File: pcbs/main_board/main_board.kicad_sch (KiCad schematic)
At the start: 6 parts, among them J3 LED strip, J4 Motor, P1 USB/STEPUP, U1 mini_esp32

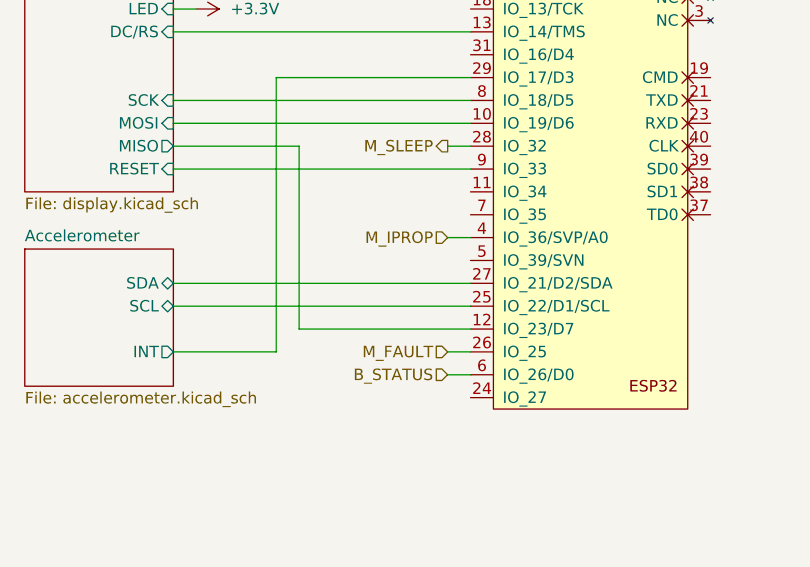
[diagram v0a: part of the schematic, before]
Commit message: Changed pinout
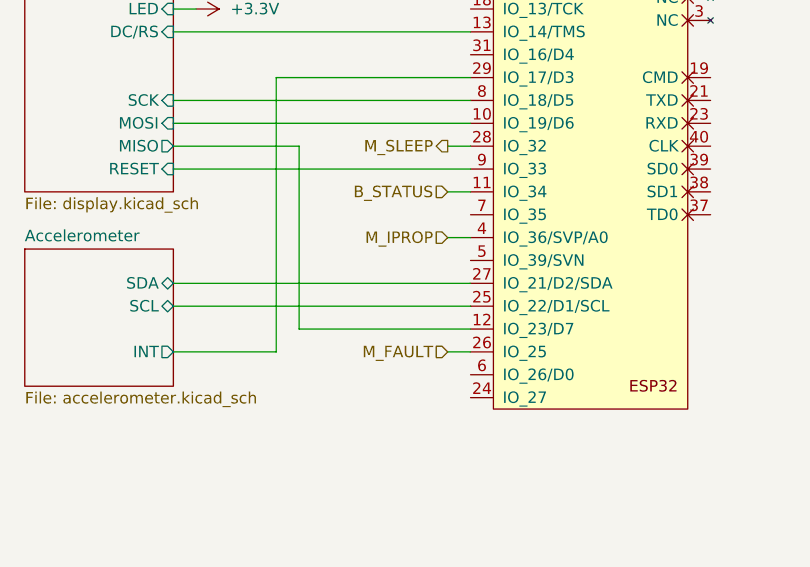
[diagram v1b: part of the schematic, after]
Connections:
- net B_STATUS: now also U1.11 (IO_34); no longer U1.6 (IO_26/D0)
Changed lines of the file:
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@@
 	(wire
 		(pts
-			(xy 133.35 100.33) (xy 135.89 100.33)
-		)
-		(stroke
-			(width 0)
-			(type default)
-		)
-	)
-	(wire
-		(pts
 			(xy 121.92 34.29) (xy 121.92 46.99)
 		)
@@
 	(wire
 		(pts
+			(xy 133.35 80.01) (xy 135.89 80.01)
+		)
+		(stroke
+			(width 0)
+			(type default)
+		)
+	)
+	(wire
+		(pts
 			(xy 177.8 39.37) (xy 177.8 49.53)
 		)
@@
 	(hierarchical_label "B_STATUS"
 		(shape input)
-		(at 133.35 100.33 180)
+		(at 133.35 80.01 180)
 		(effects
 			(font

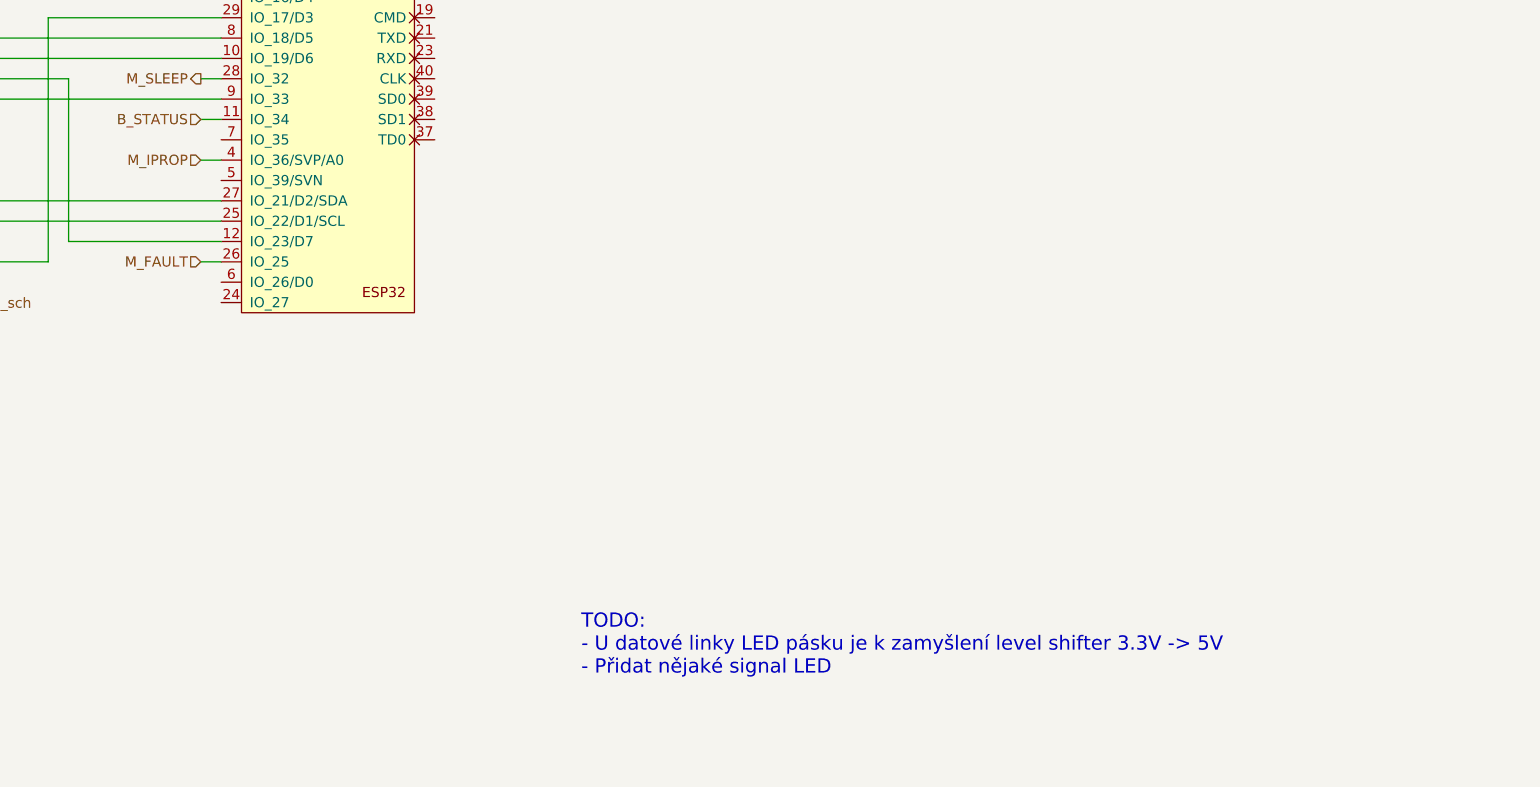
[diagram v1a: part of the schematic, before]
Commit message: ID pins, BOM, fuse
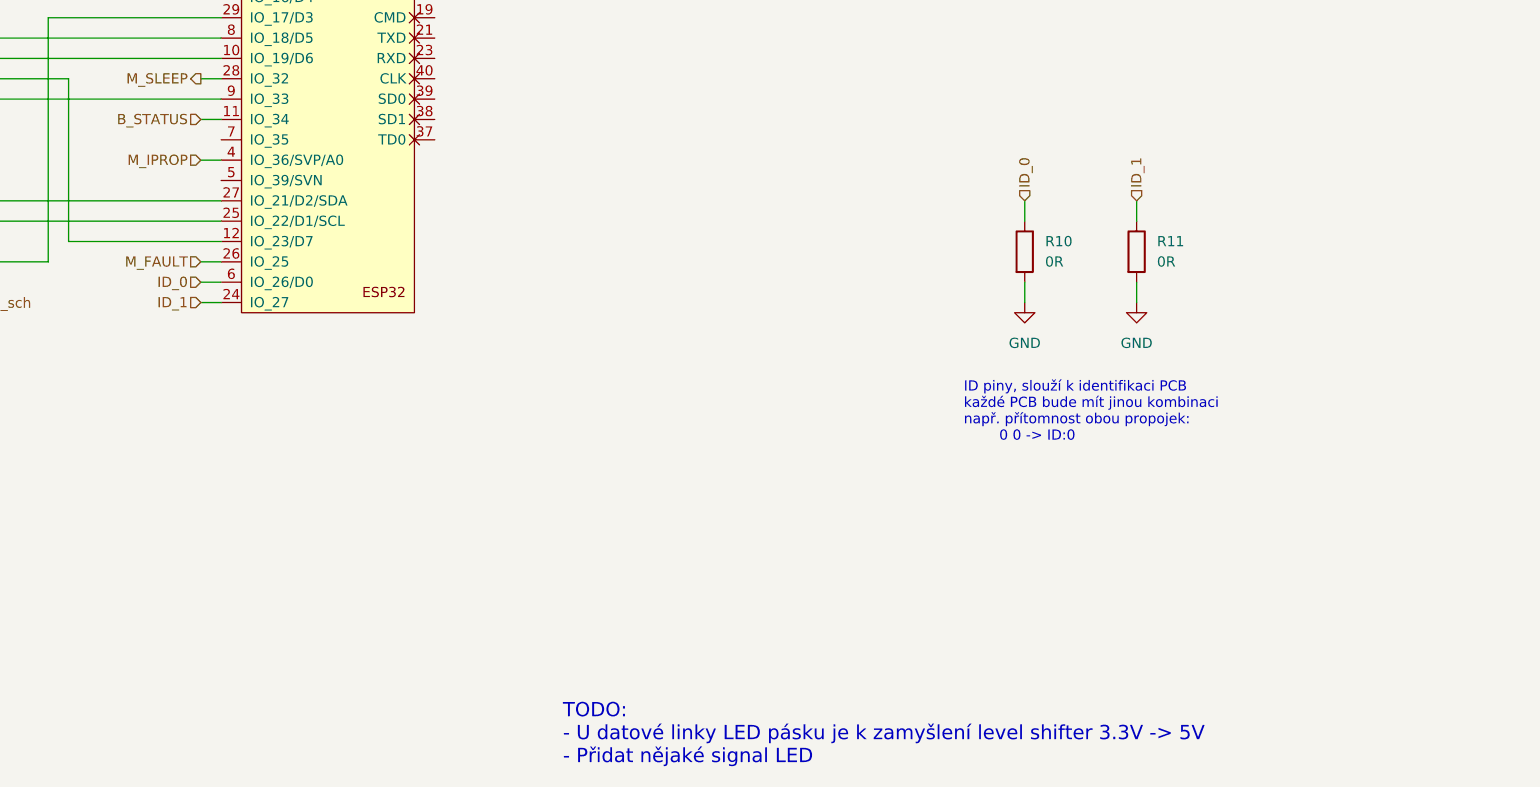
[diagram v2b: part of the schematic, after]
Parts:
- added R10, R11: 0R, Resistor_SMD:R_0603_1608Metric_Pad0.98x0.95mm_HandSolder, symbol Device:R
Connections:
- net GND: now also R10.2, R11.2
- net ID_1: now reaches U1.24 (IO_27)
- net ID_1: now also R11.1
- net ID_0: now reaches U1.6 (IO_26/D0)
- net ID_0: now also R10.1
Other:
- note added: "ID piny, slouží k identifikaci PCB každé PCB bude mít jinou kombinaci např. přítomnost obou propojek: 0 0 -> ID:0"

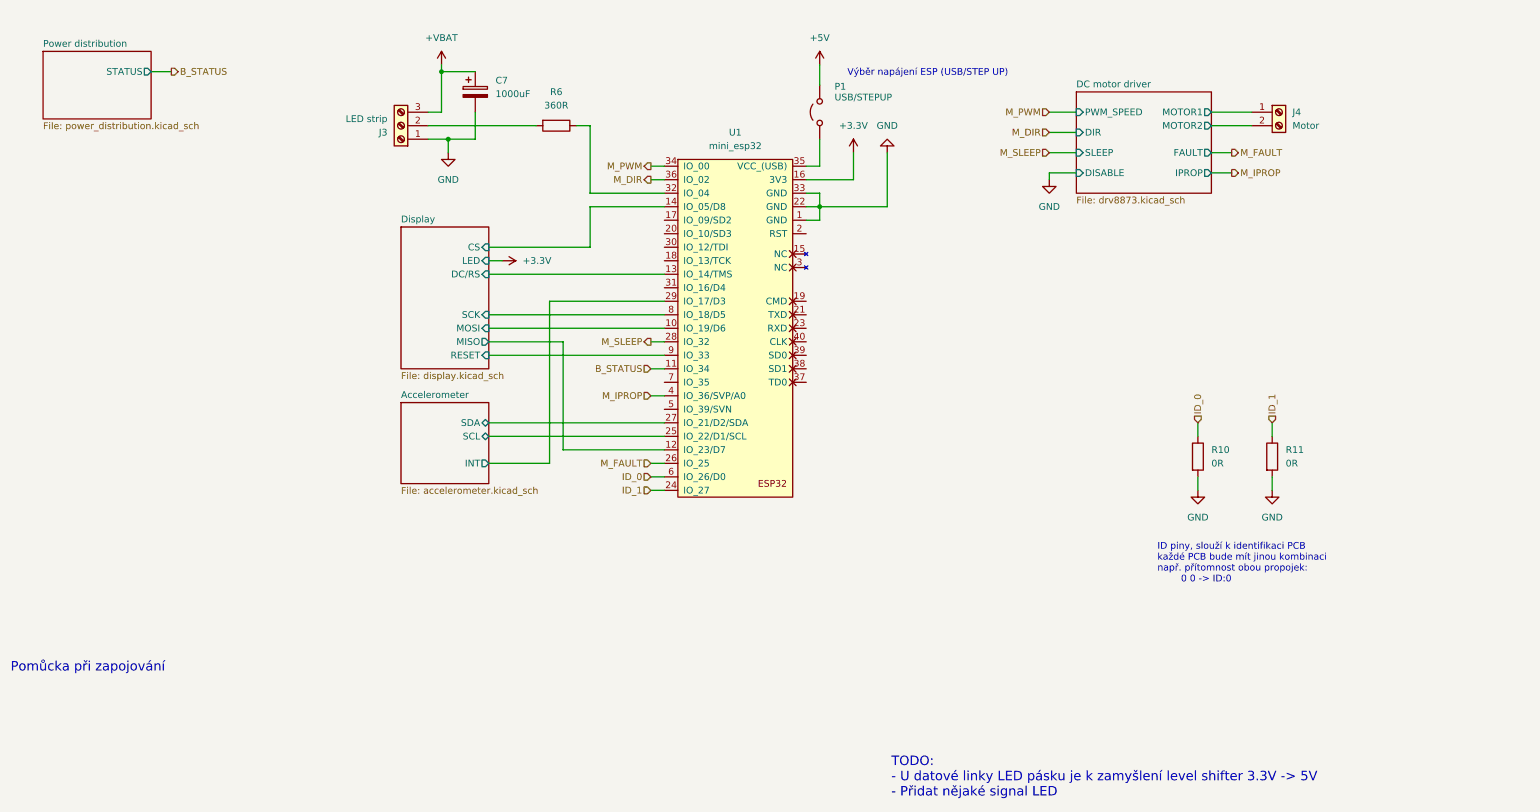
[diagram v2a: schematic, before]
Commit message: ESP power update
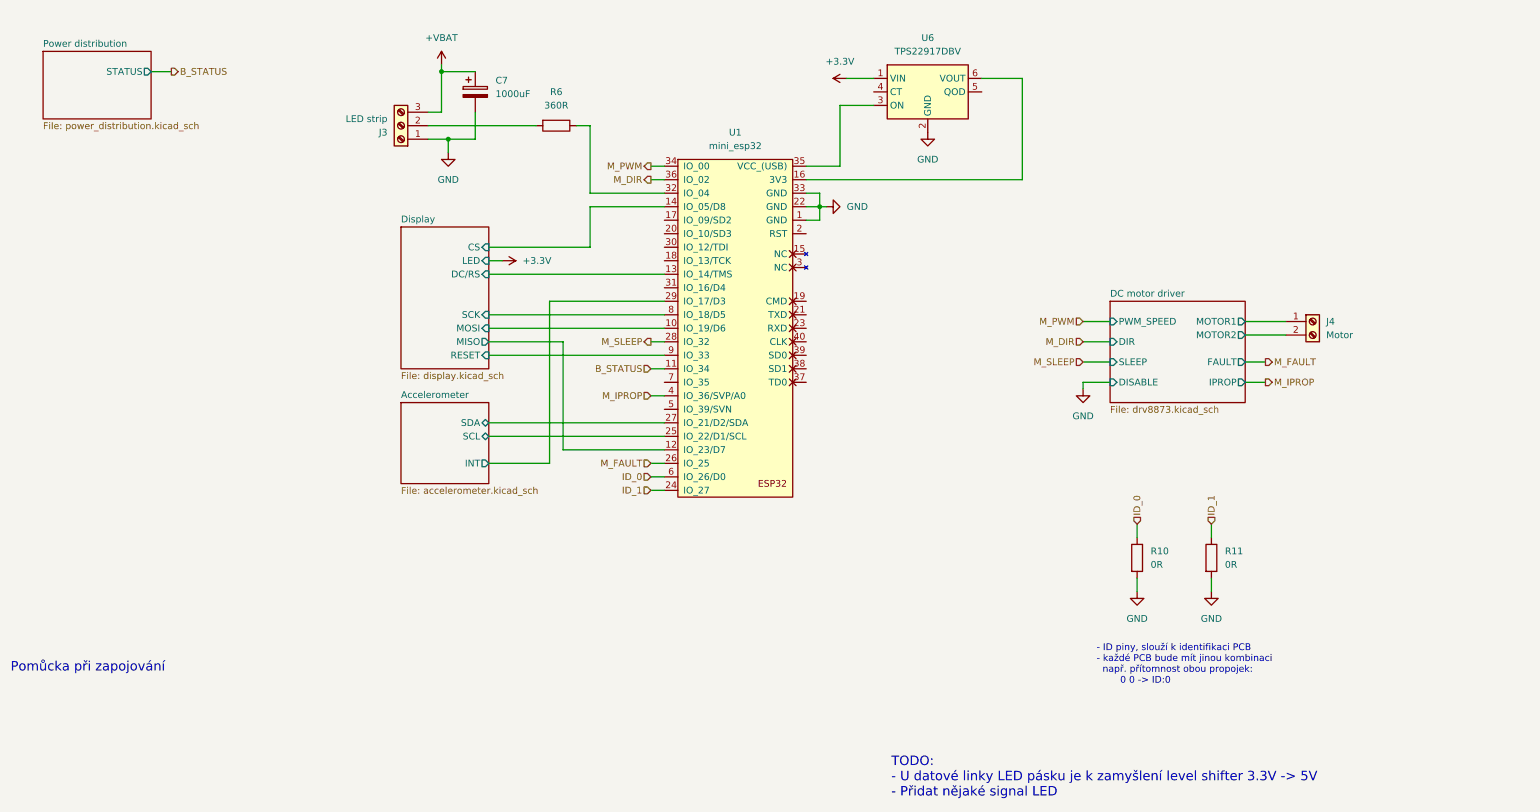
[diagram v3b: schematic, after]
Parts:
- removed P1: USB/STEPUP, Connector_PinHeader_2.54mm:PinHeader_1x03_P2.54mm_Horizontal, symbol Jumper:Jumper_2_Open
- added U6: TPS22917DBV, Package_TO_SOT_SMD:SOT-23-6, symbol Power_Management:TPS22917DBV
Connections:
- net +3.3V: now also U6.1 (VIN); no longer U1.16 (3V3)
- net GND: now also U6.2 (GND)
- net at U1.35 (VCC_(USB)): now also U6.3 (ON)
- new net: U1.16 (3V3), U6.6 (VOUT)
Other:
- note added: "- ID piny, slouží k identifikaci PCB - každé PCB bude mít jinou kombinaci např. přítomnost obou propojek: 0 0 -> ID:0"
- note removed: "ID piny, slouží k identifikaci PCB každé PCB bude mít jinou kombinaci např. přítomnost obou propojek: 0 0 -> ID:0"
- note removed: "Výběr napájení ESP (USB/STEP UP)"
- moved on the sheet: J4, R10, R11

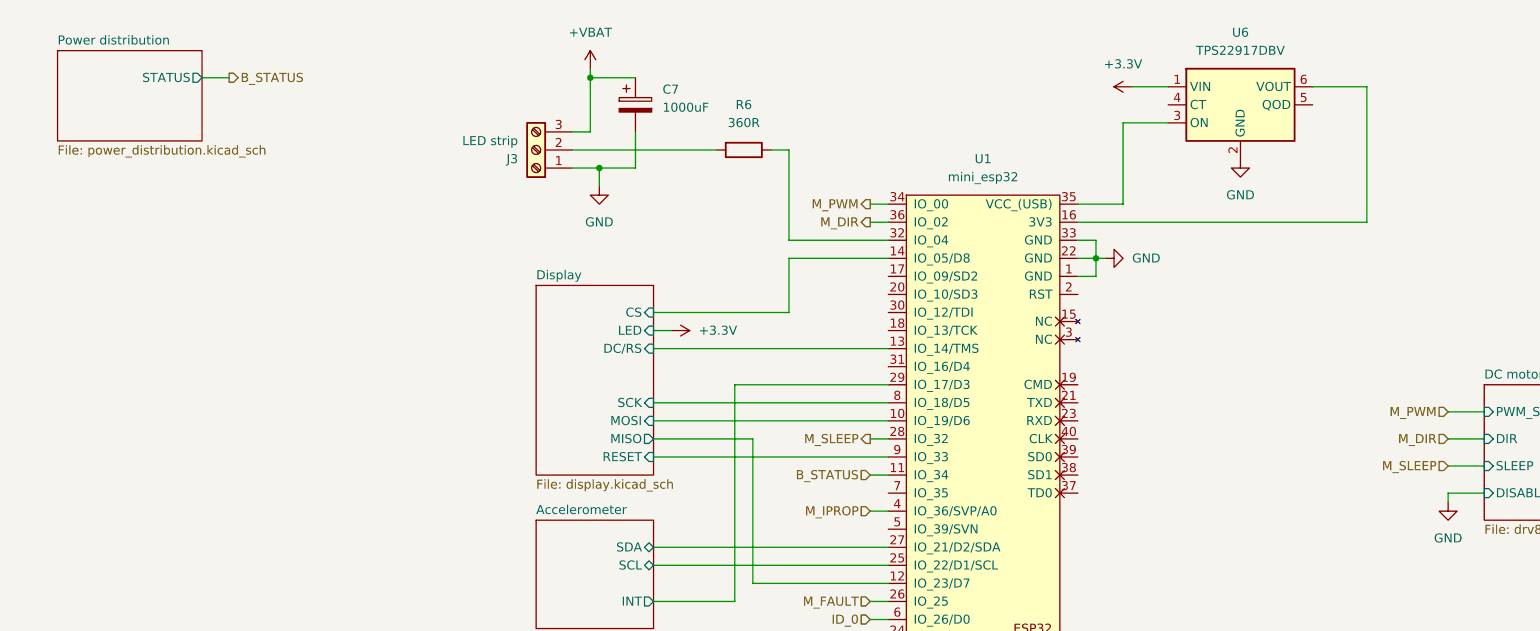
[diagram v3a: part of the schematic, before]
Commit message: Add IC for charging
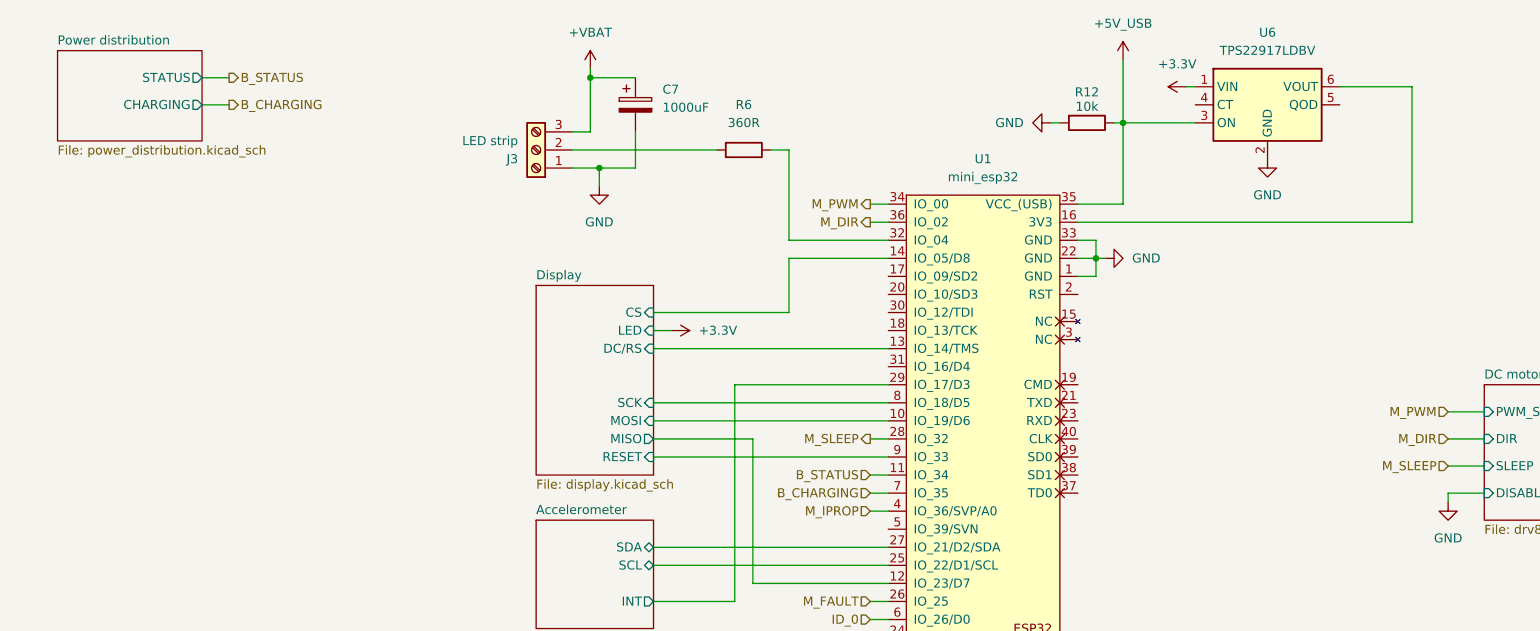
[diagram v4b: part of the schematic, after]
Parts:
- added R12: 10k, Resistor_SMD:R_0603_1608Metric_Pad0.98x0.95mm_HandSolder, symbol Device:R
- U6: value TPS22917DBV -> TPS22917LDBV
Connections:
- net GND: now also R12.2
- net +5V_USB: now reaches U1.35 (VCC_(USB)), U6.3 (ON)
- net +5V_USB: now also R12.1
- net B_CHARGING: now reaches U1.7 (IO_35)
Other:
- sheet Power distribution ports: added CHARGING; removed none
- moved on the sheet: U6

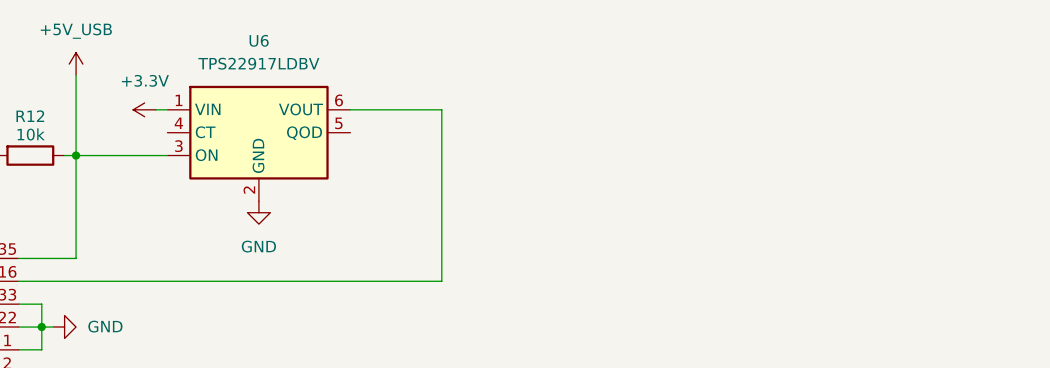
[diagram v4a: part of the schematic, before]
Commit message: Add 3V3 regulator
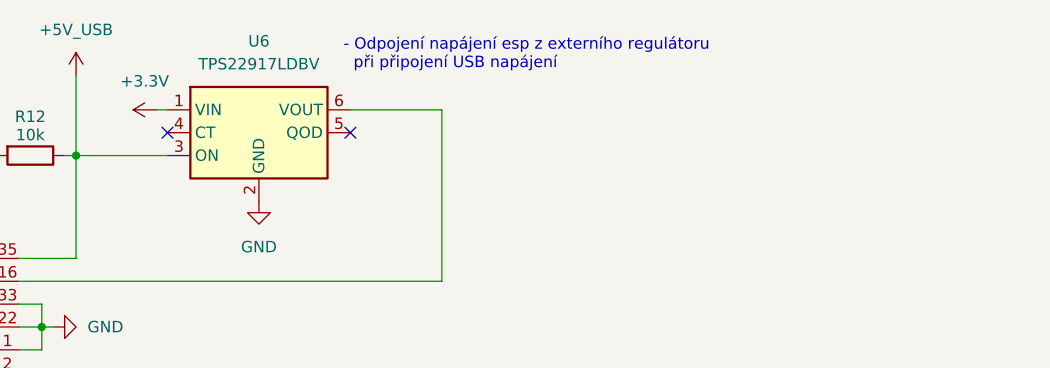
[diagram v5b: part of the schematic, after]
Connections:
- no-connect marks 0 -> 2
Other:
- note added: "- Odpojení napájení esp z externího regulátoru při připojení USB napájení"
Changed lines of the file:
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@@
+		)
+	)
+	(text "- Odpojení napájení esp z externího regulátoru\n  při připojení USB napájení\n"
+		(exclude_from_sim no)
+		(at 198.628 17.526 0)
+		(effects
+			(font
+				(size 1.27 1.27)
+			)
+			(justify left top)
 		)
 	)
@@
 		(color 0 0 0 0)
 	)
+	(no_connect
+		(at 179.07 27.94)
+	)
+	(no_connect
+		(at 199.39 27.94)
+	)
 	(wire
